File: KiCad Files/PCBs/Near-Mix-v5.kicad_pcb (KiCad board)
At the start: 2 copper layers, 60.6 x 46 mm, 80 parts, among them J1 Conn_01x03_Male, J2 Conn_01x03_Female, J3 Conn_01x03_Male, J4 Conn_01x03_Female, U1 TL072, U2 TL072

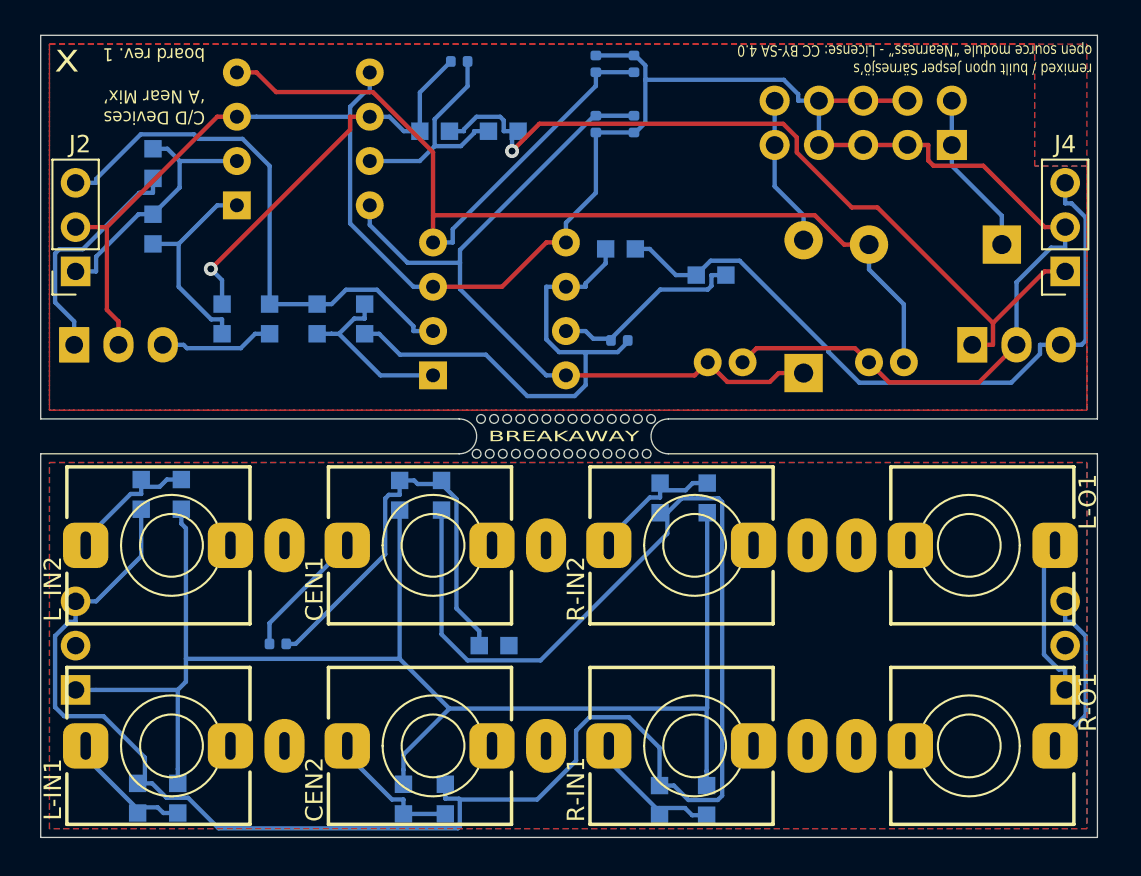
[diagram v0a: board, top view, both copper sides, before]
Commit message: first fully SMD version ordered from JLCPCB 2024-10-24
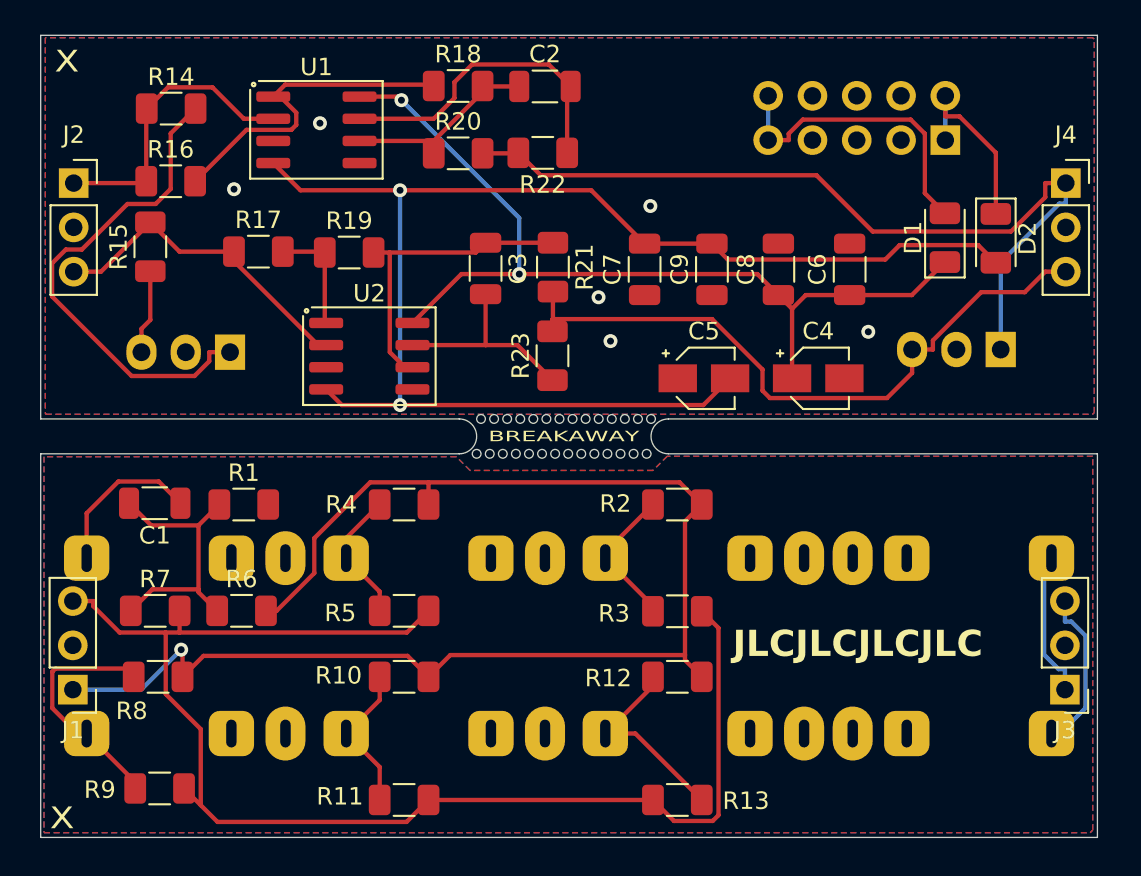
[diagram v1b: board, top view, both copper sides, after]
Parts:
- removed logo: , Graphics
- C1, C2, C3, C6, C7, C8, C9: footprint Capacitor_SMD:C_0402_1005Metric -> Capacitor_SMD:C_1206_3216Metric; moved to F.Cu
- C4, C5: footprint Capacitor_THT:C_Radial_D5.0mm_H11.0mm_P2.00mm -> Capacitor_SMD:CP_Elec_3x5.3; moved to F.Cu
- CEN1, CEN2, L-IN1, L-O1, L_IN2, R-IN1, R-IN2, R-O1: footprint AudioJacks:Jack_3.5mm_QingPu_WQP-PJ398SM_Vertical -> Audio Jacks:Jack_3.5mm_QingPu_WQP-PJ398SM_Vertical; moved to B.Cu
- D1, D2: footprint Diode_THT:D_DO-41_SOD81_P7.62mm_Horizontal -> Diode_SMD:D_1206_3216Metric; moved to F.Cu
- J1, J3: moved to F.Cu
- PWR1: footprint Connector_IDC:IDC-Header_2x05_P2.54mm_Vertical -> Connector_PinHeader_2.54mm:PinHeader_2x05_P2.54mm_Vertical
- R1, R10, R11, R12, R13, R14, R15, R16, R17, R18, R19, R2, R20, R21, R22, R23, R3, R4, R5, R6, R7, R8, R9: footprint PCM_4ms_Resistor:R_0603 -> PCM_4ms_Resistor:R_1206_3216Metric; moved to F.Cu
- U1, U2: footprint Package_DIP:DIP-8_W7.62mm_Socket -> PCM_Package_SO_AKL:SOIC-8_3.9x4.9mm_P1.27mm; moved to F.Cu
- moved R3 31.5 mm to (154.0, 111.3), turned to 0 degrees
- moved L_IN2 29.8 mm to (154.8, 108.2), turned to -90 degrees
- moved R2 28.5 mm to (154.0, 105.1), turned to 0 degrees
- moved R4 21.3 mm to (138.3, 105.1), turned to 0 degrees
- moved R18 19.0 mm to (141.4, 81.1), turned to 0 degrees
- moved R10 18.7 mm to (138.3, 115.0), turned to 0 degrees
- moved R5 18.7 mm to (138.3, 111.2), turned to 0 degrees
- moved L-IN1 18.4 mm to (139.9, 108.2), turned to -90 degrees
- moved R7 17.7 mm to (124.0, 111.2), turned to 0 degrees
- moved R13 17.4 mm to (154.0, 122.1), turned to 180 degrees
- moved R1 16.5 mm to (129.1, 105.1)
- moved R9 16.4 mm to (124.3, 121.4), turned to 0 degrees
- moved R8 15.7 mm to (124.2, 115.0), turned to 0 degrees
- moved R-IN1 15.1 mm to (139.9, 118.3), turned to -90 degrees
- moved CEN1 15.0 mm to (125.0, 108.2), turned to -90 degrees
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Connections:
- net Net-(C1-Pad1) renamed /CEN_IN_1_net
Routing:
- net GND: track 127.1 -> 0.00 mm, vias 0 -> 6
- net Net-(J1-Pin_3): track 112.0 -> 78.5 mm
- net Net-(ST-IN1-Pin_1): track 13.6 -> 28.6 mm
- net Net-(J2-Pin_3): track 31.9 -> 18.9 mm
- net -12V: track 68.1 -> 81.0 mm, vias 0 -> 2
- net Net-(U1B--): track 23.4 -> 11.4 mm, vias 1 -> 0
- net Net-(U2B--): track 29.5 -> 17.9 mm
- net Net-(C1-Pad2): track 25.6 -> 15.9 mm
- net Net-(D1-A): track 8.69 -> 17.6 mm
- net +12V: track 45.4 -> 53.7 mm, vias 0 -> 2
- net Net-(R16-Pad2): track 12.3 -> 19.1 mm
- net Net-(CEN2-PadT): track 8.02 -> 13.9 mm
- net Net-(C2-Pad2): track 13.2 -> 18.3 mm
- net Net-(R17-Pad2): track 10.3 -> 6.50 mm
- net Net-(R-IN2-PadT): track 8.01 -> 11.5 mm
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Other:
- board text added: "A Near Mix"
- board text added: "Common Denominator Devices"
- board text added: "board rev. ${revision}"
- board text added: "remixed / built upon Jesper Särnesjö’s open source module “Nearness” License: CC BY-SA 4.0"
- board text removed: "C/D Devices ‘A Near Mix’ board rev. 1"
- board text removed: "remixed / built upon Jesper Särnesjö’s open source module “Nearness” - License: CC BY-SA 4.0"

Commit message: uses different footprint for diodes - JLC didn't have parts to match previous updates labels so they are oriented sanely and not cut off by pads ordered 2024-10-25 order for previous commit cancelled
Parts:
- D1, D2: footprint Diode_SMD:D_1206_3216Metric -> Diode_SMD:D_SOD-123F
